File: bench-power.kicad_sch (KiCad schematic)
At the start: 36 parts, among them J1 16PIN, J2 CV_IN, J3 GATE_IN, J4 POWER_IN

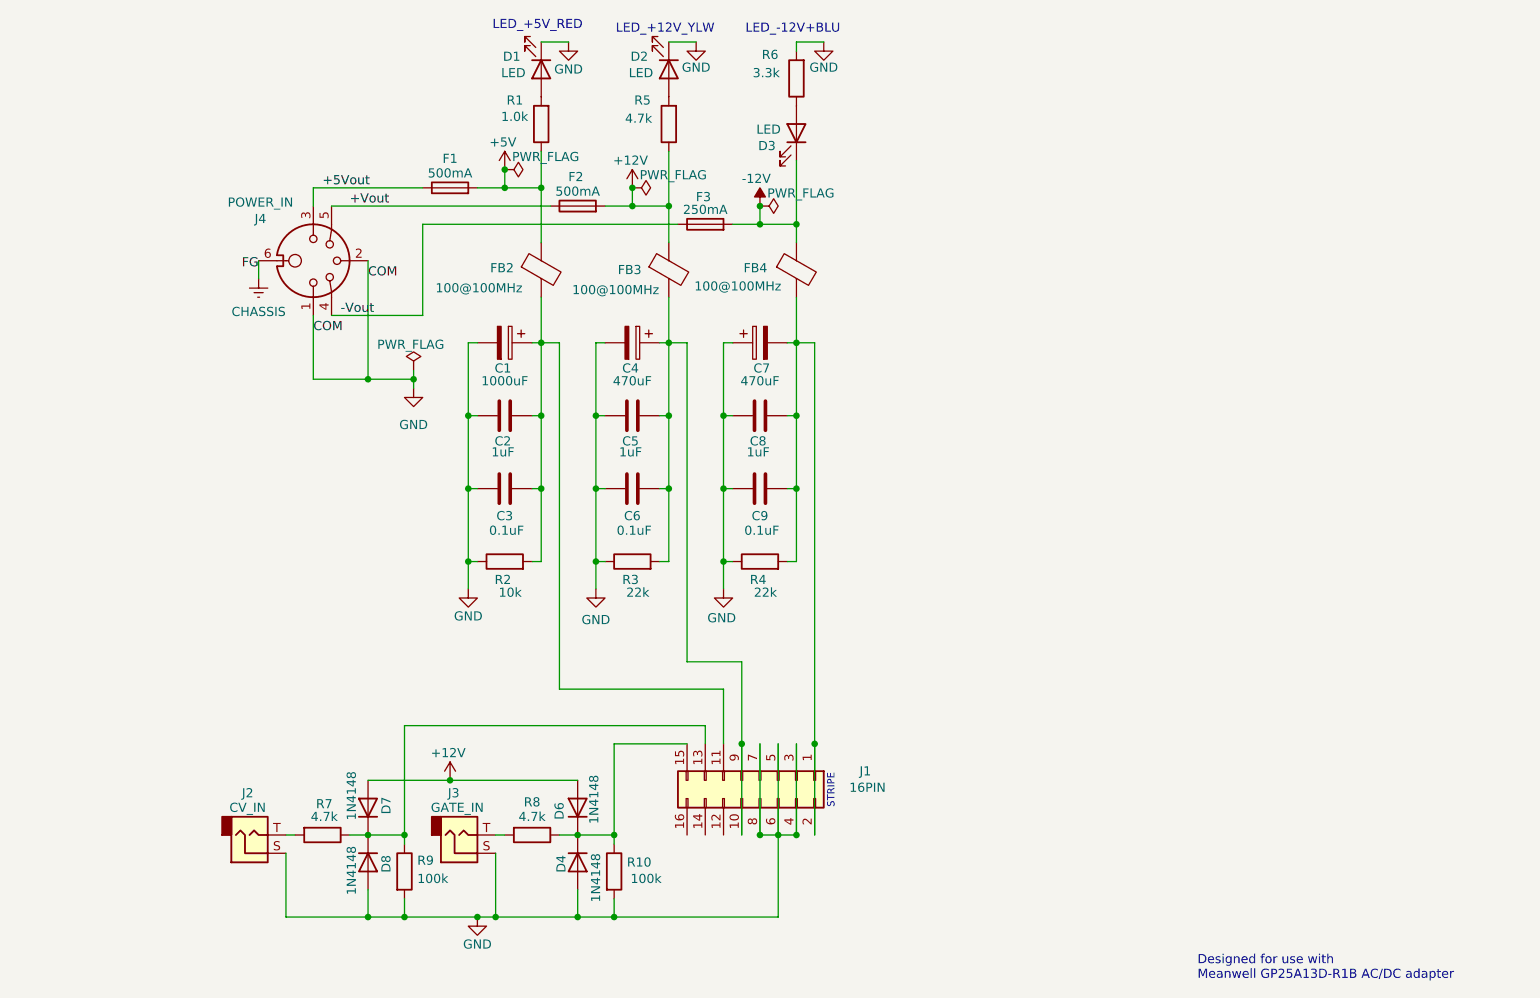
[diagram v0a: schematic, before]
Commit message: banana jack output
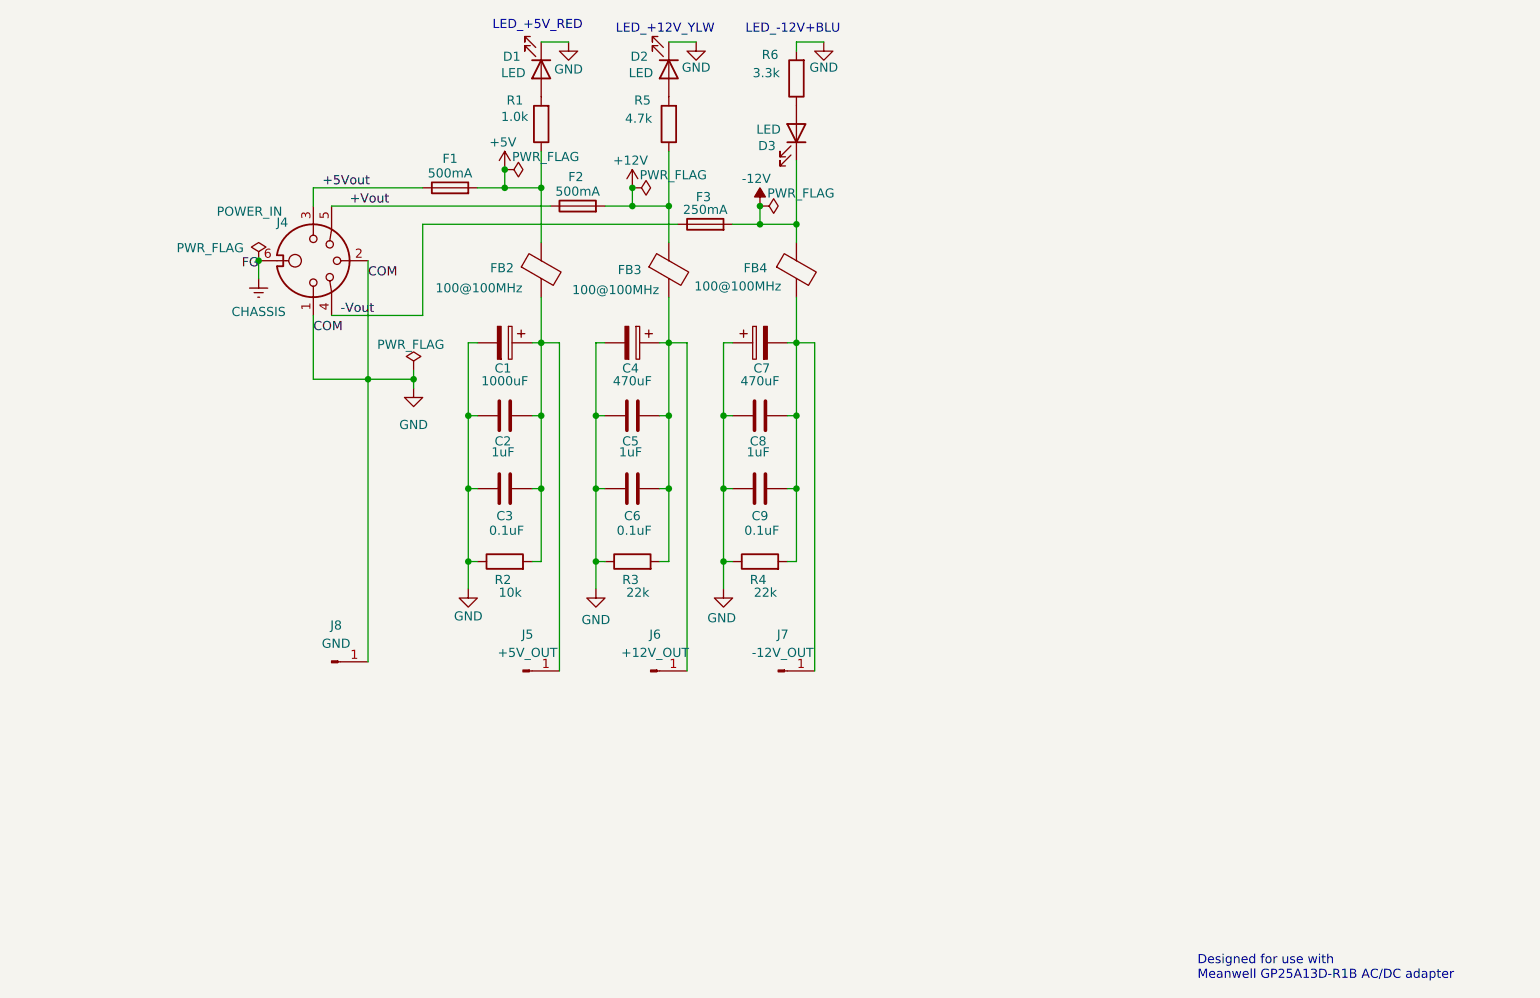
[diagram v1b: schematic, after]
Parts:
- removed D4, D6, D7, D8: 1N4148, Diode_THT:D_DO-35_SOD27_P7.62mm_Horizontal, symbol Diode:1N4148
- removed J1: 16PIN, Connector_IDC:IDC-Header_2x08-1MP_P2.54mm_Latch_Vertical, symbol Connector_Generic:Conn_02x08_Odd_Even
- removed J2: CV_IN, symbol Connector_Audio:AudioJack2
- removed J3: GATE_IN, symbol Connector_Audio:AudioJack2
- removed R10, R9: 100k, Resistor_THT:R_Axial_DIN0204_L3.6mm_D1.6mm_P5.08mm_Horizontal, symbol Device:R
- removed R7, R8: 4.7k, Resistor_THT:R_Axial_DIN0204_L3.6mm_D1.6mm_P5.08mm_Horizontal, symbol Device:R
- added J5: +5V_OUT, symbol Connector:Conn_01x01_Pin
- added J6: +12V_OUT, symbol Connector:Conn_01x01_Pin
- added J7: -12V_OUT, symbol Connector:Conn_01x01_Pin
- added J8: GND, symbol Connector:Conn_01x01_Pin
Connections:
- net GND: now also J8.1 (Pin_1)
- net at C1.1, C2.2, C3.2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: now also J5.1 (Pin_1)
- net at C7.2, C8.2, C9.2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: now also J7.1 (Pin_1)
- net at C4.1, C5.2, C6.2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: now also J6.1 (Pin_1)
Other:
- note removed: "STRIPE"

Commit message: prototype candidate
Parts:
- removed J5: +5V_OUT, symbol Connector:Conn_01x01_Pin
- removed J6: +12V_OUT, symbol Connector:Conn_01x01_Pin
- removed J7: -12V_OUT, symbol Connector:Conn_01x01_Pin
- removed J8: GND, symbol Connector:Conn_01x01_Pin
- added J1: PWR_OUT, Connector_JST:JST_XH_B4B-XH-A_1x04_P2.50mm_Vertical, symbol Connector:Conn_01x04_Pin
- added J2: POWER_IN_BRD, Connector_JST:JST_XH_B5B-XH-A_1x05_P2.50mm_Vertical, symbol Connector:Conn_01x05_Pin
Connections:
- net +5Vout: now also J2.3 (Pin_3)
- net +Vout: now also J2.5 (Pin_5)
- net -Vout: now also J2.4 (Pin_4)
- net GND: now also J1.1 (Pin_1), J2.1 (Pin_1), J2.2 (Pin_2)
- net at C1.1, C2.2, C3.2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: now also J1.2 (Pin_2)
- net at C7.2, C8.2, C9.2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: now also J1.4 (Pin_4)
- net at C4.1, C5.2, C6.2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: now also J1.3 (Pin_3)
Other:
- moved on the sheet: J4

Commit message: wip
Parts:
- added TP1: GND, symbol Connector:TestPoint
- added TP2: +5V, symbol Connector:TestPoint
- added TP3: +12V, symbol Connector:TestPoint
- added TP4: -12V, symbol Connector:TestPoint
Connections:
- net GND: now also TP1.1
- net at C1.1, C2.2, C3.2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: now also TP2.1
- net at C7.2, C8.2, C9.2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: now also TP4.1
- net at C4.1, C5.2, C6.2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: now also TP3.1

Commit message: test points
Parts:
- TP1, TP2, TP3, TP4: footprint (none) -> TestPoint:TestPoint_Pad_D1.0mm
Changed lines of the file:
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@@
 			)
 		)
-		(property "Footprint" ""
+		(property "Footprint" "TestPoint:TestPoint_Pad_D1.0mm"
 			(at 105.41 128.27 0)
 			(effects
@@
 			)
 		)
-		(property "Footprint" ""
+		(property "Footprint" "TestPoint:TestPoint_Pad_D1.0mm"
 			(at 123.19 130.81 0)
 			(effects
@@
 			)
 		)
-		(property "Footprint" ""
+		(property "Footprint" "TestPoint:TestPoint_Pad_D1.0mm"
 			(at 88.9 125.73 0)
 			(effects
@@
 			)
 		)
-		(property "Footprint" ""
+		(property "Footprint" "TestPoint:TestPoint_Pad_D1.0mm"
 			(at 63.5 116.84 0)
 			(effects

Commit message: wip
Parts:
- added J3: LOAD, Connector_JST:JST_XH_B4B-XH-A_1x04_P2.50mm_Vertical, symbol Connector:Conn_01x04_Pin
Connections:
- net +5Vout: now also J3.3 (Pin_3)
- net +Vout: now also J3.1 (Pin_1)
- net -Vout: now also J3.2 (Pin_2)
- net GND: now also J3.4 (Pin_4)
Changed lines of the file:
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@@
 	)
 	(junction
+		(at 59.69 67.31)
+		(diameter 0)
+		(color 0 0 0 0)
+	)
+	(junction
 		(at 82.55 59.69)
 		(diameter 0)
@@
 	)
 	(junction
+		(at 63.5 106.68)
+		(diameter 0)
+		(color 0 0 0 0)
+	)
+	(junction
 		(at 105.41 93.98)
 		(diameter 0)
@@
 	)
 	(junction
+		(at 60.96 69.85)
+		(diameter 0)
+		(color 0 0 0 0)
+	)
+	(junction
 		(at 77.47 114.3)
 		(diameter 0)
@@
 	)
 	(junction
+		(at 58.42 64.77)
+		(diameter 0)
+		(color 0 0 0 0)
+	)
+	(junction
 		(at 87.63 93.98)
 		(diameter 0)
@@
 	(wire
 		(pts
-			(xy 55.88 67.31) (xy 106.68 67.31)
+			(xy 63.5 88.9) (xy 63.5 106.68)
 		)
 		(stroke
@@
 	(wire
 		(pts
-			(xy 55.88 64.77) (xy 88.9 64.77)
+			(xy 55.88 64.77) (xy 58.42 64.77)
 		)
 		(stroke
@@
 	(wire
 		(pts
-			(xy 121.92 114.3) (xy 123.19 114.3)
+			(xy 60.96 104.14) (xy 60.96 69.85)
 		)
 		(stroke
@@
 	(wire
 		(pts
-			(xy 123.19 58.42) (xy 123.19 67.31)
+			(xy 121.92 114.3) (xy 123.19 114.3)
 		)
 		(stroke
@@
 	(wire
 		(pts
-			(xy 45.72 73.66) (xy 55.88 73.66)
+			(xy 123.19 58.42) (xy 123.19 67.31)
 		)
 		(stroke
@@
 	(wire
 		(pts
-			(xy 55.88 82.55) (xy 55.88 74.93)
+			(xy 45.72 73.66) (xy 55.88 73.66)
 		)
 		(stroke
@@
 	(wire
 		(pts
-			(xy 87.63 83.82) (xy 87.63 93.98)
+			(xy 55.88 82.55) (xy 55.88 74.93)
 		)
 		(stroke
@@
 	(wire
 		(pts
-			(xy 55.88 69.85) (xy 67.31 69.85)
+			(xy 87.63 83.82) (xy 87.63 93.98)
 		)
 		(stroke
@@
 	(wire
 		(pts
+			(xy 58.42 99.06) (xy 58.42 64.77)
+		)
+		(stroke
+			(width 0)
+			(type default)
+		)
+	)
+	(wire
+		(pts
 			(xy 95.25 93.98) (xy 95.25 104.14)
 		)
@@
 	(wire
 		(pts
+			(xy 59.69 101.6) (xy 59.69 67.31)
+		)
+		(stroke
+			(width 0)
+			(type default)
+		)
+	)
+	(wire
+		(pts
 			(xy 48.26 68.58) (xy 55.88 68.58)
 		)
@@
 	(wire
 		(pts
-			(xy 86.36 104.14) (xy 87.63 104.14)
+			(xy 59.69 67.31) (xy 106.68 67.31)
 		)
 		(stroke
@@
 	(wire
 		(pts
-			(xy 68.58 128.27) (xy 68.58 133.35)
+			(xy 86.36 104.14) (xy 87.63 104.14)
 		)
 		(stroke
@@
 	(wire
 		(pts
-			(xy 105.41 57.15) (xy 105.41 64.77)
+			(xy 68.58 128.27) (xy 68.58 133.35)
 		)
 		(stroke
@@
 	(wire
 		(pts
-			(xy 55.88 74.93) (xy 63.5 74.93)
+			(xy 105.41 57.15) (xy 105.41 64.77)
 		)
 		(stroke
@@
 	(wire
 		(pts
-			(xy 107.95 83.82) (xy 107.95 128.27)
+			(xy 55.88 74.93) (xy 63.5 74.93)
 		)
 		(stroke
@@
 	(wire
 		(pts
-			(xy 63.5 88.9) (xy 63.5 121.92)
+			(xy 107.95 83.82) (xy 107.95 128.27)
 		)
 		(stroke
@@
 	(wire
 		(pts
+			(xy 55.88 67.31) (xy 59.69 67.31)
+		)
+		(stroke
+			(width 0)
+			(type default)
+		)
+	)
+	(wire
+		(pts
 			(xy 105.41 83.82) (xy 105.41 93.98)
 		)
@@
 	(wire
 		(pts
+			(xy 55.88 99.06) (xy 58.42 99.06)
+		)
+		(stroke
+			(width 0)
+			(type default)
+		)
+	)
+	(wire
+		(pts
 			(xy 118.11 67.31) (xy 123.19 67.31)
 		)
@@
 	(wire
 		(pts
+			(xy 55.88 104.14) (xy 60.96 104.14)
+		)
+		(stroke
+			(width 0)
+			(type default)
+		)
+	)
+	(wire
+		(pts
 			(xy 69.85 88.9) (xy 69.85 90.17)
 		)
@@
 	(wire
 		(pts
+			(xy 55.88 106.68) (xy 63.5 106.68)
+		)
+		(stroke
+			(width 0)
+			(type default)
+		)
+	)
+	(wire
+		(pts
 			(xy 113.03 93.98) (xy 113.03 104.14)
 		)
@@
 	(wire
 		(pts
+			(xy 63.5 106.68) (xy 63.5 121.92)
+		)
+		(stroke
+			(width 0)
+			(type default)
+		)
+	)
+	(wire
+		(pts
 			(xy 125.73 83.82) (xy 125.73 130.81)
 		)
@@
 	(wire
 		(pts
+			(xy 55.88 101.6) (xy 59.69 101.6)
+		)
+		(stroke
+			(width 0)
+			(type default)
+		)
+	)
+	(wire
+		(pts
 			(xy 96.52 64.77) (xy 100.33 64.77)
 		)
@@
 	(wire
 		(pts
+			(xy 58.42 64.77) (xy 88.9 64.77)
+		)
+		(stroke
+			(width 0)
+			(type default)
+		)
+	)
+	(wire
+		(pts
 			(xy 86.36 93.98) (xy 87.63 93.98)
 		)
@@
 	(wire
 		(pts
+			(xy 55.88 69.85) (xy 60.96 69.85)
+		)
+		(stroke
+			(width 0)
+			(type default)
+		)
+	)
+	(wire
+		(pts
 			(xy 77.47 114.3) (xy 78.74 114.3)
 		)
@@
 	(wire
 		(pts
+			(xy 60.96 69.85) (xy 67.31 69.85)
+		)
+		(stroke
+			(width 0)
+			(type default)
+		)
+	)
+	(wire
+		(pts
 			(xy 63.5 72.39) (xy 63.5 74.93)
 		)
@@
 					(unit 1)
 				)
+			)
+		)
+	)
+	(symbol
+		(lib_id "Connector:Conn_01x04_Pin")
+		(at 50.8 101.6 0)
+		(unit 1)
+		(exclude_from_sim no)
+		(in_bom yes)
+		(on_board yes)
+		(dnp no)
+		(property "Reference" "J3"
+			(at 51.435 93.98 0)
+			(effects
+				(font
+					(size 1.27 1.27)
+				)
+			)
+		)
+		(property "Value" "LOAD"
+			(at 51.435 96.52 0)
+			(effects
+				(font
+					(size 1.27 1.27)
+				)
+			)
+		)
+		(property "Footprint" "Connector_JST:JST_XH_B4B-XH-A_1x04_P2.50mm_Vertical"
+			(at 50.8 101.6 0)
+			(effects
+				(font
+					(size 1.27 1.27)
+				)
+				(hide yes)
+			)
+		)
+		(property "Datasheet" "~"
+			(at 50.8 101.6 0)
+			(effects
+				(font
+					(size 1.27 1.27)
+				)
+				(hide yes)
+			)
+		)
+		(property "Description" "Generic connector, single row, 01x04, script generated"
+			(at 50.8 101.6 0)
+			(effects
+				(font
+					(size 1.27 1.27)
+				)
+				(hide yes)
+			)
+		)
+		(pin "2"
+		)
+		(pin "1"
+		)
+		(pin "4"
+		)
+		(pin "3"
+		)
+		(instances
+			(project ""
+				(path "/7d945acc-eebf-4bd3-96a2-bce5a0d85bfc"
+					(reference "J3")
+					(unit 1)
+				)
